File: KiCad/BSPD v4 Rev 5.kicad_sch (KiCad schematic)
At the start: 194 parts, among them J1 DTM13-12PA, U1 LM339, U10 2N7002, U11 2N7002, U12 2N7002, U13 2N7002, U14 2N7002, U15 2N7002, U16 2N7002, U17 74HC08D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

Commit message: moved lm393 to 12v
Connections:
- net +12V: now also C17.1, U27.8 (V+)
- net +5V: no longer C17.1, U27.8 (V+)
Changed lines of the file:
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@@
 	)
 	(junction
+		(at 261.62 36.83)
+		(diameter 0)
+		(color 0 0 0 0)
+	)
+	(junction
 		(at 158.75 227.33)
 		(diameter 0)
@@
 	)
 	(junction
-		(at 250.19 36.83)
-		(diameter 0)
-		(color 0 0 0 0)
-	)
-	(junction
 		(at 68.58 368.3)
 		(diameter 0)
@@
 	)
 	(junction
-		(at 261.62 36.83)
-		(diameter 0)
-		(color 0 0 0 0)
-	)
-	(junction
 		(at 25.4 38.1)
 		(diameter 0)
@@
 	)
 	(junction
+		(at 261.62 21.59)
+		(diameter 0)
+		(color 0 0 0 0)
+	)
+	(junction
 		(at 149.86 273.05)
 		(diameter 0)
@@
 	)
 	(junction
-		(at 250.19 21.59)
-		(diameter 0)
-		(color 0 0 0 0)
-	)
-	(junction
 		(at 132.08 165.1)
 		(diameter 0)
@@
 	)
 	(junction
-		(at 261.62 21.59)
-		(diameter 0)
-		(color 0 0 0 0)
-	)
-	(junction
 		(at 68.58 170.18)
 		(diameter 0)
@@
 	(wire
 		(pts
-			(xy 250.19 16.51) (xy 250.19 21.59)
+			(xy 250.19 16.51) (xy 250.19 25.4)
 		)
 		(stroke
@@
 	(wire
 		(pts
-			(xy 250.19 21.59) (xy 250.19 25.4)
-		)
-		(stroke
-			(width 0)
-			(type default)
-		)
-	)
-	(wire
-		(pts
 			(xy 66.04 170.18) (xy 68.58 170.18)
 		)
@@
 	(wire
 		(pts
-			(xy 250.19 41.91) (xy 250.19 36.83)
+			(xy 250.19 33.02) (xy 250.19 41.91)
 		)
 		(stroke
@@
 	(wire
 		(pts
-			(xy 250.19 36.83) (xy 250.19 33.02)
-		)
-		(stroke
-			(width 0)
-			(type default)
-		)
-	)
-	(wire
-		(pts
 			(xy 142.24 17.78) (xy 162.56 17.78)
 		)
@@
 	(wire
 		(pts
-			(xy 250.19 36.83) (xy 261.62 36.83)
-		)
-		(stroke
-			(width 0)
-			(type default)
-		)
-	)
-	(wire
-		(pts
 			(xy 128.27 26.67) (xy 128.27 17.78)
 		)
@@
 	(wire
 		(pts
-			(xy 250.19 21.59) (xy 261.62 21.59)
-		)
-		(stroke
-			(width 0)
-			(type default)
-		)
-	)
-	(wire
-		(pts
 			(xy 233.68 165.1) (xy 233.68 173.99)
 		)
@@
 	)
 	(symbol
+		(lib_id "power:+12V")
+		(at 261.62 21.59 0)
+		(unit 1)
+		(exclude_from_sim no)
+		(in_bom yes)
+		(on_board yes)
+		(dnp no)
+		(property "Reference" "#PWR098"
+			(at 261.62 25.4 0)
+			(effects
+				(font
+					(size 1.27 1.27)
+				)
+				(hide yes)
+			)
+		)
+		(property "Value" "+12V"
+			(at 261.62 18.034 0)
+			(effects
+				(font
+					(size 1.27 1.27)
+				)
+			)
+		)
+		(property "Footprint" ""
+			(at 261.62 21.59 0)
+			(effects
+				(font
+					(size 1.27 1.27)
+				)
+				(hide yes)
+			)
+		)
+		(property "Datasheet" ""
+			(at 261.62 21.59 0)
+			(effects
+				(font
+					(size 1.27 1.27)
+				)
+				(hide yes)
+			)
+		)
+		(property "Description" "Power symbol creates a global label with name \"+12V\""
+			(at 261.62 21.59 0)
+			(effects
+				(font
+					(size 1.27 1.27)
+				)
+				(hide yes)
+			)
+		)
+		(pin "1"
+		)
+		(instances
+			(project "BSPD v4 Rev 5"
+				(path "/2adce50a-518b-4fe5-b442-5f6e663f213c"
+					(reference "#PWR098")
+					(unit 1)
+				)
+			)
+		)
+	)
+	(symbol
 		(lib_id "Custom_connectors:Test_hook")
 		(at 36.83 115.57 270)
@@
 					(unit 1)
 				)
+			)
+		)
+	)
+	(symbol
+		(lib_id "power:GND")
+		(at 261.62 36.83 0)
+		(unit 1)
+		(exclude_from_sim no)
+		(in_bom yes)
+		(on_board yes)
+		(dnp no)
+		(property "Reference" "#PWR099"
+			(at 261.62 43.18 0)
+			(effects
+				(font
+					(size 1.27 1.27)
+				)
+				(hide yes)
+			)
+		)
+		(property "Value" "GND"
+			(at 261.62 40.386 0)
+			(effects
+				(font
+					(size 1.27 1.27)
+				)
+			)
+		)
+		(property "Footprint" ""
+			(at 261.62 36.83 0)
+			(effects
+				(font
+					(size 1.27 1.27)
+				)
+				(hide yes)
+			)
+		)
+		(property "Datasheet" ""
+			(at 261.62 36.83 0)
+			(effects
+				(font
+					(size 1.27 1.27)
+				)
+				(hide yes)
+			)
+		)
+		(property "Description" "Power symbol creates a global label with name \"GND\" , ground"
+			(at 261.62 36.83 0)
+			(effects
+				(font
+					(size 1.27 1.27)
+				)
+				(hide yes)
+			)
+		)
+		(pin "1"
+		)
+		(instances
+			(project "BSPD v4 Rev 5"
+				(path "/2adce50a-518b-4fe5-b442-5f6e663f213c"
+					(reference "#PWR099")
+					(unit 1)
+				)

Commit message: differentail TPS, stable Over ref voltage
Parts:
- added C20: C0.33uF, Capacitor_SMD:C_0805_2012Metric_Pad1.18x1.45mm_HandSolder, symbol Device:C
- added C21: C0.1uF, Capacitor_SMD:C_0805_2012Metric_Pad1.18x1.45mm_HandSolder, symbol Device:C
- added U4: 78L08MG-AB3-R, Package_TO_SOT_SMD:SOT-89-3_Handsoldering, symbol LDO:UTC_78L08MG-AB3-R
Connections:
- net +12V: now also C20.1, U4.3 (IN); no longer R11.1, R17.1, R23.1, R5.1, RV12.1, RV3.1, RV6.1, RV9.1
- net GND: now also C20.2, C21.2, U4.2 (GND)
- net TPS2: now also U2.4 (-); no longer U2.5 (+)
- net at R10.1, R9.2, RV5.2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: now also U2.5 (+); no longer U2.4 (-)
- new net +8V: C21.1, R11.1, R17.1, R23.1, R5.1, RV12.1, RV3.1, RV6.1, RV9.1, U4.1 (OUT)
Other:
- note added: "5v Regulator"
- note added: "8v Regulator"
- note removed: "Voltage Regulator"
- moved on the sheet: C11, C15, U22

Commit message: Added support for differential input, Changed LED colors and resistor
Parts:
- added JP1, JP2, JP3, JP4: SolderJumper_3_Open, Test Hook:SolderedJumper 3P, symbol Jumper:SolderJumper_3_Open
- D1, D10, D4, D7: value LED -> YLED
- D11, D2, D5, D8: value LED -> GLED
- D12, D14, D15, D3, D6, D9: value LED -> RLED
- R49, R51, R52, R54, R55, R57, R58, R60, R77, R83: value R150 -> R200
- R50, R53, R56, R59: value R150 -> R82
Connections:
- net BRK2: now also JP3.3 (B), JP4.1 (A); no longer U3.11 (+)
- net TPS2: now also JP1.3 (B), JP2.1 (A); no longer U2.4 (-)
- net at R10.1, R9.2, RV5.2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: now also JP1.1 (A), JP2.3 (B); no longer U2.5 (+)
- net at R21.2, R22.1, RV11.2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: now also JP3.1 (A), JP4.3 (B); no longer U3.10 (-)
- new net: JP2.2 (C), U2.4 (-)
- new net: JP1.2 (C), U2.5 (+)
- new net: JP3.2 (C), U3.11 (+)
- new net: JP4.2 (C), U3.10 (-)
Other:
- moved on the sheet: TP11, TP7

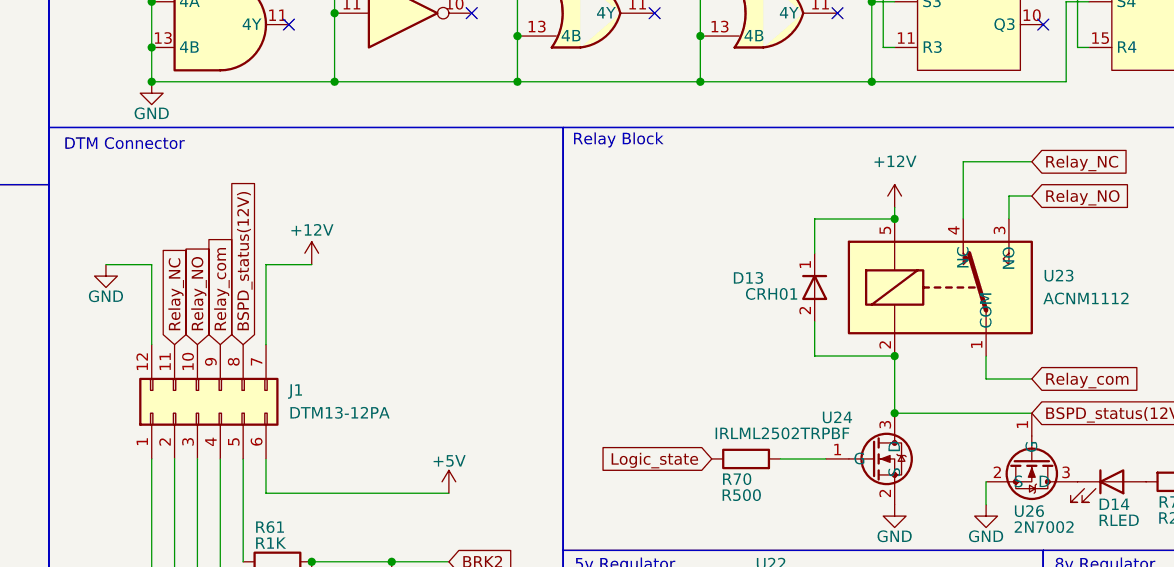
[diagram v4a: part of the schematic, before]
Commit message: Fixed, swapped relay symbol swapped NC and NO (same wiring maintained)
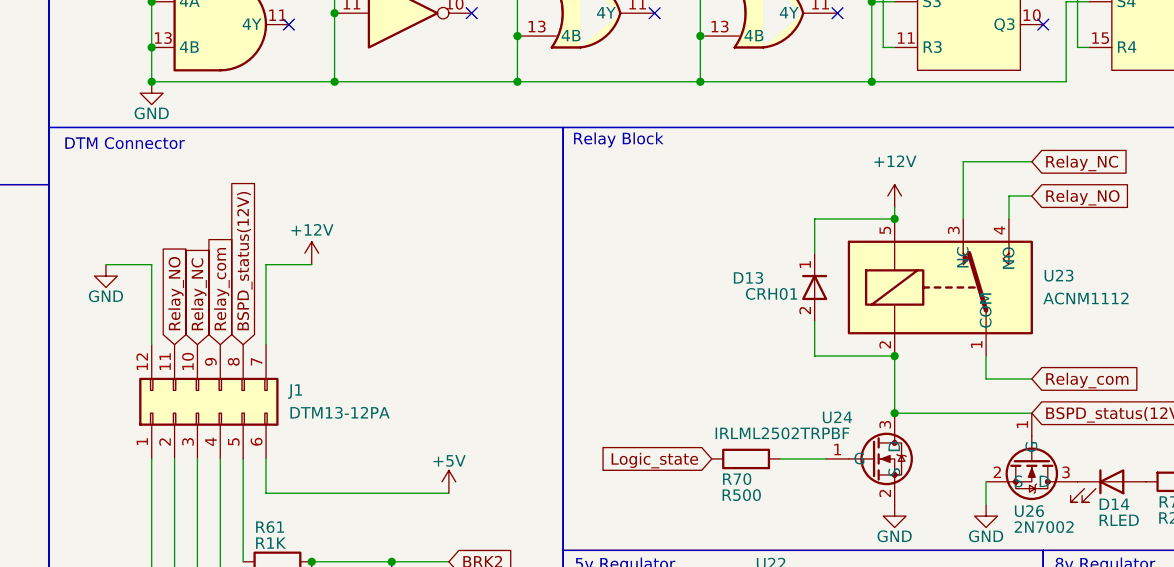
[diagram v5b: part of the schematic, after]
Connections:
- net Relay_NC: now also J1.10, U23.3 (NC); no longer J1.11, U23.4 (NC)
- net Relay_NO: now also J1.11, U23.4 (NO); no longer J1.10, U23.3 (NO)
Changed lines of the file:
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@@
 	(global_label "Relay_NO"
 		(shape input)
-		(at 137.16 203.2 90)
+		(at 134.62 203.2 90)
 		(fields_autoplaced yes)
 		(effects
@@
 		)
 		(property "Intersheetrefs" "${INTERSHEET_REFS}"
-			(at 137.16 191.4458 90)
+			(at 134.62 191.4458 90)
 			(effects
 				(font
@@
 	(global_label "Relay_NC"
 		(shape input)
-		(at 134.62 203.2 90)
+		(at 137.16 203.2 90)
 		(fields_autoplaced yes)
 		(effects
@@
 		)
 		(property "Intersheetrefs" "${INTERSHEET_REFS}"
-			(at 134.62 191.5063 90)
+			(at 137.16 191.5063 90)
 			(effects
 				(font
@@
 			)
 		)
-		(property "Datasheet" "https://www.lcsc.com/product-detail/C5355536.html"
+		(property "Datasheet" "https://lcsc.com/product-detail/Automotive-Relays_PANASONIC-ACNM1112_C5355536.html"
 			(at 209.55 189.23 0)
 			(effects

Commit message: fixed fuckup
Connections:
- net BRK2: now also U3.11 (+); no longer U3.7 (+)
- net TPS2: now also U2.5 (+); no longer U1.9 (+)
- net at R7.2, R8.1, RV4.2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: now also JP1.1 (A), JP2.3 (B); no longer U1.8 (-)
- net at R10.1, R9.2, RV5.2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: now also U2.4 (-); no longer JP1.1 (A), JP2.3 (B)
- net at JP2.2 (C): now also U1.8 (-); no longer U2.4 (-)
- net at JP1.2 (C): now also U1.9 (+); no longer U2.5 (+)
- net at R21.2, R22.1, RV11.2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: now also U3.10 (-); no longer JP3.1 (A), JP4.3 (B)
- net at JP3.2 (C): now also U3.7 (+); no longer U3.11 (+)
- net at R19.2, R20.1, RV10.2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: now also JP3.1 (A), JP4.3 (B); no longer U3.6 (-)
- net at JP4.2 (C): now also U3.6 (-); no longer U3.10 (-)
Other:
- moved on the sheet: JP1, JP2, JP3, JP4, TP11, TP14, TP16, TP2, TP4, TP7
